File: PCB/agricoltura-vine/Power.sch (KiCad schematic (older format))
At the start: 23 parts

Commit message: Power supplies
Both power supplies redsigned around new ICs for 2A of each voltage, since we have no idea how much current peripherals will be using.
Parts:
- removed C?: GRM21BD70J226ME44L, growbox-KiCAD-Capacitors:C0805, symbol AVR-KiCAD-Lib-Capacitors:GRM21BD70J226ME44L
- removed C?: CGA3E2X7R1H104K080AA, AVR-KiCAD-Lib-Capacitors:C0603, symbol AVR-KiCAD-Lib-Capacitors:CGA3E2X7R1H104K080AA
- removed C?: GRM31CR71H475KA12L, growbox-KiCAD-Capacitors:C1206, symbol AVR-KiCAD-Lib-Capacitors:GRM31CR71H475KA12L
- removed C?: GRM32EC72A106KE05L, AVR-KiCAD-Lib-Capacitors:C1210, symbol AVR-KiCAD-Lib-Capacitors:GRM32EC72A106KE05L
- removed C?: C3216X5R1V156M160AC, AVR-KiCAD-Lib-Capacitors:C1206, symbol AVR-KiCAD-Lib-Capacitors:C3216X5R1V156M160AC
- removed C?: C2012X7R2A104K125AA, AVR-KiCAD-Lib-Capacitors:C0805, symbol AVR-KiCAD-Lib-Capacitors:C2012X7R2A104K125AA
- removed L?: SDR0403-120ML, AVR-KiCAD-Lib-Inductors:SDR0403-120ML, symbol AVR-KiCAD-Lib-Inductors:SDR0403-120ML
- removed L?: SDR0604-180YL, AVR-KiCAD-Lib-Inductors:INDP5858X480N, symbol AVR-KiCAD-Lib-Inductors:SDR0604-180YL
- removed R? (x2): RC0402FR-0722K1L, AVR-KiCAD-Lib-Resistors:R0402, symbol AVR-KiCAD-Lib-Resistors:RC0402FR-0722K1L
- removed R?: RC0402FR-07412KL, AVR-KiCAD-Lib-Resistors:R0402, symbol AVR-KiCAD-Lib-Resistors:RC0402FR-07412KL
- removed R?: RC0402FR-0751KL, AVR-KiCAD-Lib-Resistors:R0402, symbol AVR-KiCAD-Lib-Resistors:RC0402FR-0751KL
- removed R?: RC0402FR-07200KL, AVR-KiCAD-Lib-Resistors:R0402, symbol AVR-KiCAD-Lib-Resistors:RC0402FR-07200KL
- removed R?: RC0402FR-07750KL, AVR-KiCAD-Lib-Resistors:R0402, symbol AVR-KiCAD-Lib-Resistors:RC0402FR-07750KL
- removed R?: CRCW0402294KFKED, AVR-KiCAD-Lib-Resistors:R0402, symbol AVR-KiCAD-Lib-Resistors:CRCW0402294KFKED
- removed R?: RC0402FR-0788K7L, AVR-KiCAD-Lib-Resistors:R0402, symbol AVR-KiCAD-Lib-Resistors:RC0402FR-0788K7L
- removed U? (x2): TPS560430XDBVR, growbox-KiCAD-ICs:SOT-23-6_Handsoldering, symbol AVR-KiCAD-Lib-ICs:TPS560430XDBVR
- added C? (x2): GRM21BD70J226ME44L, growbox-KiCAD-Capacitors:C0805, symbol AVR-KiCAD-Lib-Capacitors:GRM21BD70J226ME44L
- added C? (x2): GRT31CR61H106KE01L, AVR-KiCAD-Lib-Capacitors:C1206, symbol AVR-KiCAD-Lib-Capacitors:GRT31CR61H106KE01L
- added C? (x2): GRT31CC81C226KE01L, AVR-KiCAD-Lib-Capacitors:C1206, symbol AVR-KiCAD-Lib-Capacitors:GRT31CC81C226KE01L
- added C? (x2): UUQ1H470MCL1GS, AVR-KiCAD-Lib-Capacitors:CP_Elec_8x10, symbol AVR-KiCAD-Lib-Capacitors:UUQ1H470MCL1GS
- added L?: SRP6540-4R7M, AVR-KiCAD-Lib-Inductors:SRP6540-4R7M, symbol AVR-KiCAD-Lib-Inductors:SRP6540-4R7M
- added L?: ASPI-0628-3R9M-T1, AVR-KiCAD-Lib-Inductors:ASPI-0628-3R9M-T1, symbol AVR-KiCAD-Lib-Inductors:ASPI-0628-3R9M-T1
- added U?: AP63205WU-7, AVR-KiCAD-Lib-ICs:SOT-23-6_Handsoldering, symbol AVR-KiCAD-Lib-ICs:AP63205WU-7
- added U?: AP63203WU-7, AVR-KiCAD-Lib-ICs:SOT-23-6_Handsoldering, symbol AVR-KiCAD-Lib-ICs:AP63203WU-7
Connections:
- wire segments 51 -> 49
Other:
- moved on the sheet: C?, D?, T?

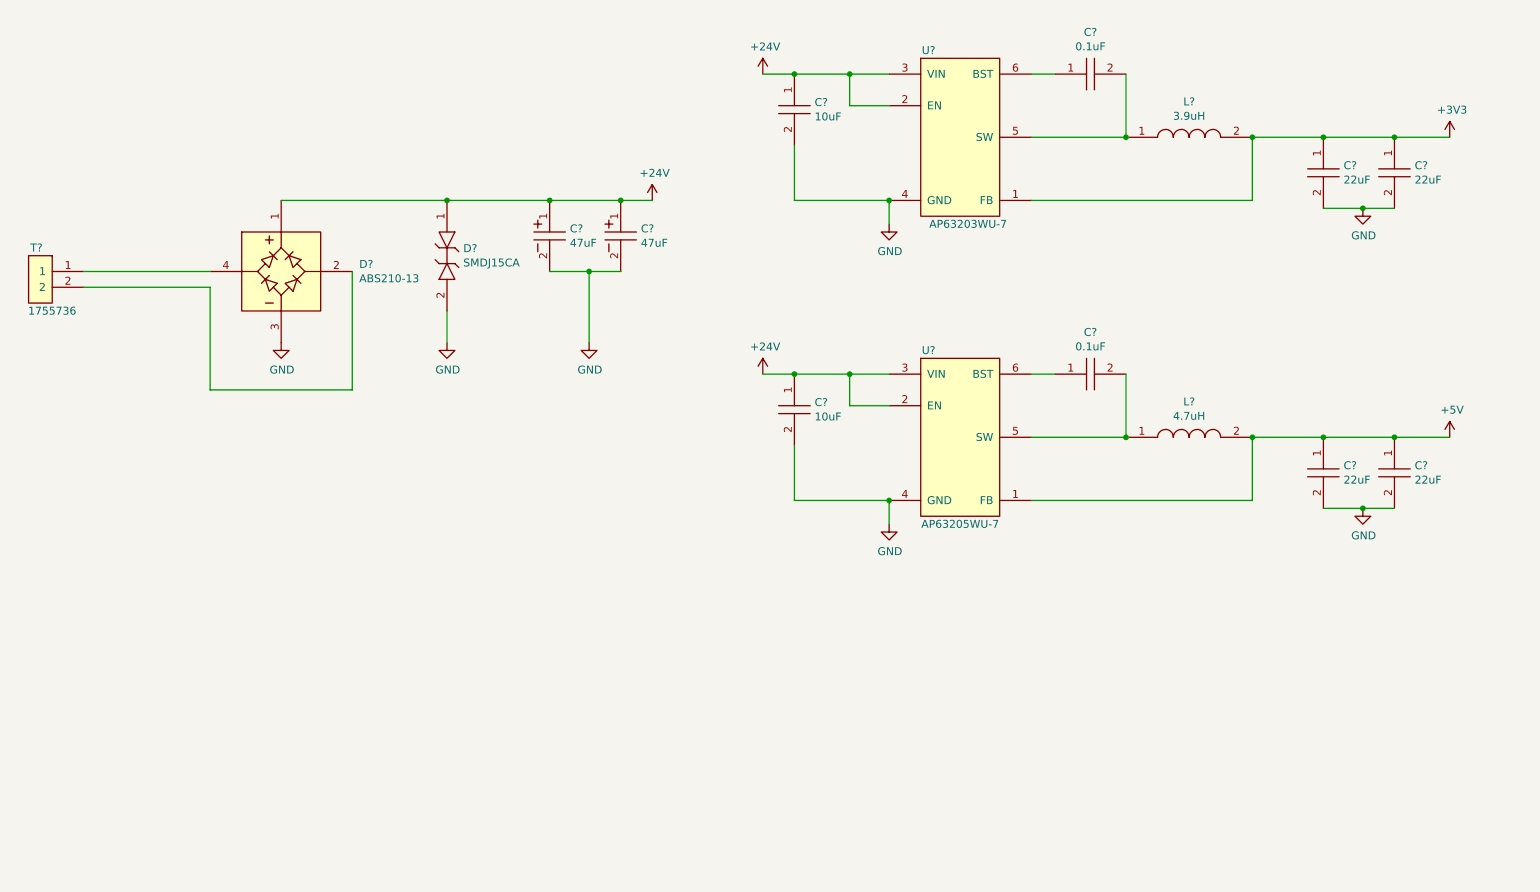
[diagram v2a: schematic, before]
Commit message: Board
Board shape defined, though subject to change. Schematic anotated and parts exported to board.
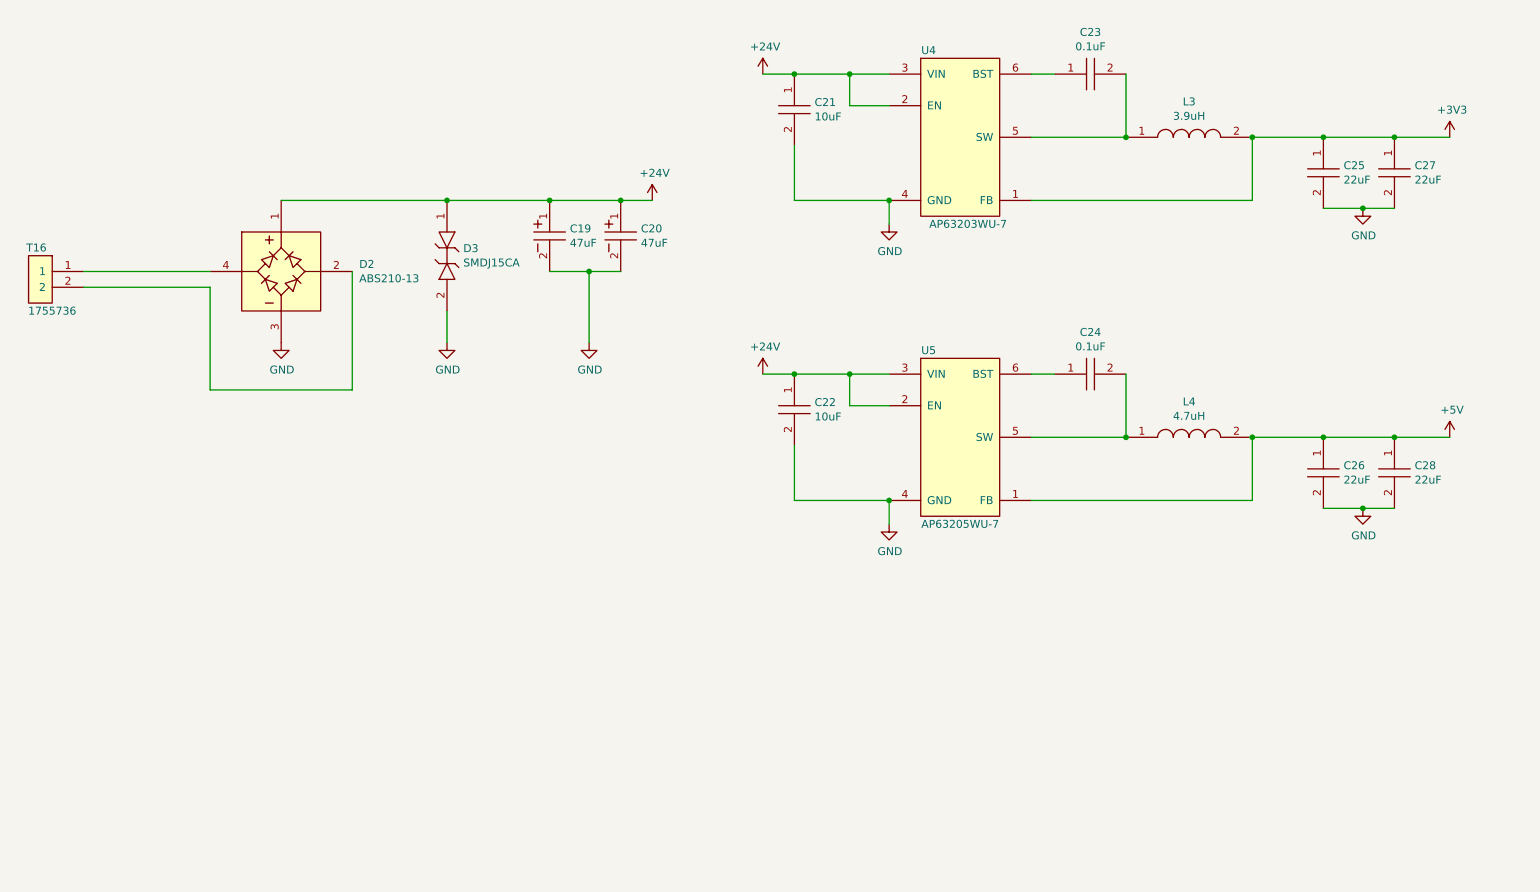
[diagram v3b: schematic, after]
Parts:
- gave numbers to parts that had none: 17
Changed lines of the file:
@@
 $EndDescr
 $Comp
-L AVR-KiCAD-Lib-Connectors:1755736 T?
+L AVR-KiCAD-Lib-Connectors:1755736 T16
 U 1 1 5EEBB45B
 P 1200 3300
-F 0 "T?" H 1300 3250 50  0000 C CNN
+F 0 "T16" H 1300 3250 50  0000 C CNN
 F 1 "1755736" H 1200 2850 50  0000 C CNN
 F 2 "growbox-KiCAD-Connectors:PhoenixContact_MSTBVA-G_02x5.08mm_Vertical" H 1000 3300 50  0001 C CNN
@@
 $EndComp
 $Comp
-L AVR-KiCAD-Lib-Diodes:ABS210-13 D?
+L AVR-KiCAD-Lib-Diodes:ABS210-13 D2
 U 1 1 5EEC167B
 P 2400 3250
-F 0 "D?" H 3144 3046 50  0000 L CNN
+F 0 "D2" H 3144 3046 50  0000 L CNN
 F 1 "ABS210-13" H 2650 4100 50  0001 C CNN
 F 2 "AVR-KiCAD-Lib-Diodes:ABS210-13" V 2800 3150 50  0001 C CNN
@@
 	3100 4250 3100 3500
 $Comp
-L power:GND #PWR?
+L power:GND #PWR028
 U 1 1 5EEC4A33
 P 2650 3950
-F 0 "#PWR?" H 2650 3700 50  0001 C CNN
+F 0 "#PWR028" H 2650 3700 50  0001 C CNN
 F 1 "GND" H 2655 3777 50  0000 C CNN
 F 2 "" H 2650 3950 50  0001 C CNN
@@
 	2650 3050 3700 3050
 $Comp
-L AVR-KiCAD-Lib-Diodes:SMDJ15CA D?
+L AVR-KiCAD-Lib-Diodes:SMDJ15CA D3
 U 1 1 5EEC73A1
 P 3700 3400
-F 0 "D?" V 3654 3503 50  0000 L CNN
+F 0 "D3" V 3654 3503 50  0000 L CNN
 F 1 "SMDJ15CA" H 3750 3600 50  0001 C CNN
 F 2 "AVR-KiCAD-Lib-Diodes:SMDJ15CA" H 3700 3300 50  0001 C CNN
@@
 $EndComp
 $Comp
-L power:GND #PWR?
+L power:GND #PWR029
 U 1 1 5EEC9E22
 P 3700 3950
-F 0 "#PWR?" H 3700 3700 50  0001 C CNN
+F 0 "#PWR029" H 3700 3700 50  0001 C CNN
 F 1 "GND" H 3705 3777 50  0000 C CNN
 F 2 "" H 3700 3950 50  0001 C CNN
@@
 	3700 3950 3700 3750
 $Comp
-L power:+24V #PWR?
+L power:+24V #PWR031
 U 1 1 5EECA5B2
 P 5000 3050
-F 0 "#PWR?" H 5000 2900 50  0001 C CNN
+F 0 "#PWR031" H 5000 2900 50  0001 C CNN
 F 1 "+24V" H 5015 3223 50  0000 C CNN
 F 2 "" H 5000 3050 50  0001 C CNN
@@
 $EndComp
 $Comp
-L AVR-KiCAD-Lib-Capacitors:C0805C104M5RACTU C?
+L AVR-KiCAD-Lib-Capacitors:C0805C104M5RACTU C23
 U 1 1 5EEE43C5
 P 7750 2250
-F 0 "C?" H 7775 2515 50  0000 C CNN
+F 0 "C23" H 7775 2515 50  0000 C CNN
 F 1 "C0805C104M5RACTU" H 7800 2450 50  0001 C CNN
 F 2 "AVR-KiCAD-Lib-Capacitors:C0805" H 7550 2250 50  0001 C CNN
@@
 $EndComp
 $Comp
-L power:+24V #PWR?
+L power:+24V #PWR033
 U 1 1 5EF02D25
 P 5700 4150
-F 0 "#PWR?" H 5700 4000 50  0001 C CNN
+F 0 "#PWR033" H 5700 4000 50  0001 C CNN
 F 1 "+24V" H 5715 4323 50  0000 C CNN
 F 2 "" H 5700 4150 50  0001 C CNN
@@
 $EndComp
 $Comp
-L power:+3V3 #PWR?
+L power:+3V3 #PWR038
 U 1 1 5EF0737A
 P 10050 2650
-F 0 "#PWR?" H 10050 2500 50  0001 C CNN
+F 0 "#PWR038" H 10050 2500 50  0001 C CNN
 F 1 "+3V3" H 10065 2823 50  0000 C CNN
 F 2 "" H 10050 2650 50  0001 C CNN
@@
 $EndComp
 $Comp
-L power:GND #PWR?
+L power:GND #PWR035
 U 1 1 5EF30432
 P 6500 5100
-F 0 "#PWR?" H 6500 4850 50  0001 C CNN
+F 0 "#PWR035" H 6500 4850 50  0001 C CNN
 F 1 "GND" H 6505 4927 50  0000 C CNN
 F 2 "" H 6500 5100 50  0001 C CNN
@@
 $EndComp
 $Comp
-L power:+5V #PWR?
+L power:+5V #PWR039
 U 1 1 5EF3A247
 P 10050 4550
-F 0 "#PWR?" H 10050 4400 50  0001 C CNN
+F 0 "#PWR039" H 10050 4400 50  0001 C CNN
 F 1 "+5V" H 10065 4723 50  0000 C CNN
 F 2 "" H 10050 4550 50  0001 C CNN
@@
 $EndComp
 $Comp
-L AVR-KiCAD-Lib-Capacitors:C2012X7R2A104K125AA C?
+L AVR-KiCAD-Lib-Capacitors:C2012X7R2A104K125AA C24
 U 1 1 5EF56247
 P 7750 4150
-F 0 "C?" H 7775 4415 50  0000 C CNN
+F 0 "C24" H 7775 4415 50  0000 C CNN
 F 1 "C2012X7R2A104K125AA" H 7800 4350 50  0001 C CNN
 F 2 "AVR-KiCAD-Lib-Capacitors:C0805" H 7550 4150 50  0001 C CNN
@@
 $EndComp
 $Comp
-L AVR-KiCAD-Lib-Capacitors:GRM21BD70J226ME44L C?
+L AVR-KiCAD-Lib-Capacitors:GRM21BD70J226ME44L C25
 U 1 1 5EEE8244
 P 9250 2850
-F 0 "C?" V 9229 2978 50  0000 L CNN
+F 0 "C25" V 9229 2978 50  0000 L CNN
 F 1 "GRM21BD70J226ME44L" H 9300 3050 50  0001 C CNN
 F 2 "growbox-KiCAD-Capacitors:C0805" H 9050 2850 50  0001 C CNN
@@
 $EndComp
 $Comp
-L AVR-KiCAD-Lib-Capacitors:GRM21BD70J226ME44L C?
+L AVR-KiCAD-Lib-Capacitors:GRM21BD70J226ME44L C27
 U 1 1 5EEE8263
 P 9700 2850
-F 0 "C?" V 9679 2978 50  0000 L CNN
+F 0 "C27" V 9679 2978 50  0000 L CNN
 F 1 "GRM21BD70J226ME44L" H 9750 3050 50  0001 C CNN
 F 2 "growbox-KiCAD-Capacitors:C0805" H 9500 2850 50  0001 C CNN
@@
 $EndComp
 $Comp
-L AVR-KiCAD-Lib-ICs:AP63205WU-7 U?
+L AVR-KiCAD-Lib-ICs:AP63205WU-7 U5
 U 1 1 5EEE9657
 P 6700 4050
-F 0 "U?" H 6750 4100 50  0000 C CNN
+F 0 "U5" H 6750 4100 50  0000 C CNN
 F 1 "AP63205WU-7" H 6750 4150 50  0001 C CNN
 F 2 "AVR-KiCAD-Lib-ICs:SOT-23-6_Handsoldering" H 5900 4700 50  0001 C CNN
@@
 $EndComp
 $Comp
-L AVR-KiCAD-Lib-Inductors:SRP6540-4R7M L?
+L AVR-KiCAD-Lib-Inductors:SRP6540-4R7M L4
 U 1 1 5EEF14B5
 P 8400 4550
-F 0 "L?" H 8400 4775 50  0000 C CNN
+F 0 "L4" H 8400 4775 50  0000 C CNN
 F 1 "SRP6540-4R7M" H 8450 4750 50  0001 C CNN
 F 2 "AVR-KiCAD-Lib-Inductors:SRP6540-4R7M" H 8400 4550 50  0001 C CNN
@@
 	6250 4150 6500 4150
 $Comp
-L power:GND #PWR?
+L power:GND #PWR037
 U 1 1 5EF0BF07
 P 9500 5000
-F 0 "#PWR?" H 9500 4750 50  0001 C CNN
+F 0 "#PWR037" H 9500 4750 50  0001 C CNN
 F 1 "GND" H 9505 4827 50  0000 C CNN
 F 2 "" H 9500 5000 50  0001 C CNN
@@
 	8800 4550 9250 4550
 $Comp
-L AVR-KiCAD-Lib-Capacitors:GRT31CR61H106KE01L C?
+L AVR-KiCAD-Lib-Capacitors:GRT31CR61H106KE01L C22
 U 1 1 5EF20097
 P 5900 4350
-F 0 "C?" V 5879 4478 50  0000 L CNN
+F 0 "C22" V 5879 4478 50  0000 L CNN
 F 1 "GRT31CR61H106KE01L" H 5950 4550 50  0001 C CNN
 F 2 "AVR-KiCAD-Lib-Capacitors:C1206" H 5700 4350 50  0001 C CNN
@@
 Connection ~ 6500 4950
 $Comp
-L AVR-KiCAD-Lib-Capacitors:GRT31CC81C226KE01L C?
+L AVR-KiCAD-Lib-Capacitors:GRT31CC81C226KE01L C26
 U 1 1 5EF26633
 P 9250 4750
-F 0 "C?" V 9229 4878 50  0000 L CNN
+F 0 "C26" V 9229 4878 50  0000 L CNN
 F 1 "GRT31CC81C226KE01L" H 9300 4950 50  0001 C CNN
 F 2 "AVR-KiCAD-Lib-Capacitors:C1206" H 9050 4750 50  0001 C CNN
@@
 	9250 4550 9700 4550
 $Comp
-L AVR-KiCAD-Lib-Capacitors:GRT31CC81C226KE01L C?
+L AVR-KiCAD-Lib-Capacitors:GRT31CC81C226KE01L C28
 U 1 1 5EF27C99
 P 9700 4750
-F 0 "C?" V 9679 4878 50  0000 L CNN
+F 0 "C28" V 9679 4878 50  0000 L CNN
 F 1 "GRT31CC81C226KE01L" H 9750 4950 50  0001 C CNN
 F 2 "AVR-KiCAD-Lib-Capacitors:C1206" H 9500 4750 50  0001 C CNN
@@
 	9700 4550 10050 4550
 $Comp
-L AVR-KiCAD-Lib-ICs:AP63203WU-7 U?
+L AVR-KiCAD-Lib-ICs:AP63203WU-7 U4
 U 1 1 5EF29865
 P 6700 2150
-F 0 "U?" H 6750 2200 50  0000 C CNN
+F 0 "U4" H 6750 2200 50  0000 C CNN
 F 1 "AP63203WU-7" H 6750 2250 50  0001 C CNN
 F 2 "AVR-KiCAD-Lib-ICs:SOT-23-6_Handsoldering" H 5900 2800 50  0001 C CNN
@@
 $EndComp
 $Comp
-L power:+24V #PWR?
+L power:+24V #PWR032
 U 1 1 5EF2E19F
 P 5700 2250
-F 0 "#PWR?" H 5700 2100 50  0001 C CNN
+F 0 "#PWR032" H 5700 2100 50  0001 C CNN
 F 1 "+24V" H 5715 2423 50  0000 C CNN
 F 2 "" H 5700 2250 50  0001 C CNN
@@
 $EndComp
 $Comp
-L power:GND #PWR?
+L power:GND #PWR034
 U 1 1 5EF2E1A5
 P 6500 3200
-F 0 "#PWR?" H 6500 2950 50  0001 C CNN
+F 0 "#PWR034" H 6500 2950 50  0001 C CNN
 F 1 "GND" H 6505 3027 50  0000 C CNN
 F 2 "" H 6500 3200 50  0001 C CNN
@@
 	6500 3200 6500 3050
 $Comp
-L AVR-KiCAD-Lib-Capacitors:GRT31CR61H106KE01L C?
+L AVR-KiCAD-Lib-Capacitors:GRT31CR61H106KE01L C21
 U 1 1 5EF2E1E9
 P 5900 2450
-F 0 "C?" V 5879 2578 50  0000 L CNN
+F 0 "C21" V 5879 2578 50  0000 L CNN
 F 1 "GRT31CR61H106KE01L" H 5950 2650 50  0001 C CNN
 F 2 "AVR-KiCAD-Lib-Capacitors:C1206" H 5700 2450 50  0001 C CNN
@@
 	7550 2250 7400 2250
 $Comp
-L AVR-KiCAD-Lib-Inductors:ASPI-0628-3R9M-T1 L?
+L AVR-KiCAD-Lib-Inductors:ASPI-0628-3R9M-T1 L3
 U 1 1 5EF379D3
 P 8400 2650
-F 0 "L?" H 8400 2875 50  0000 C CNN
+F 0 "L3" H 8400 2875 50  0000 C CNN
 F 1 "ASPI-0628-3R9M-T1" H 8450 2850 50  0001 C CNN
 F 2 "AVR-KiCAD-Lib-Inductors:ASPI-0628-3R9M-T1" H 8400 2650 50  0001 C CNN
@@
 	8800 3050 8800 2650
 $Comp
-L power:GND #PWR?
+L power:GND #PWR036
 U 1 1 5EF3F029
 P 9500 3100
-F 0 "#PWR?" H 9500 2850 50  0001 C CNN
+F 0 "#PWR036" H 9500 2850 50  0001 C CNN
 F 1 "GND" H 9505 2927 50  0000 C CNN
 F 2 "" H 9500 3100 50  0001 C CNN
@@
 	3700 3050 4350 3050
 $Comp
-L AVR-KiCAD-Lib-Capacitors:UUQ1H470MCL1GS C?
+L AVR-KiCAD-Lib-Capacitors:UUQ1H470MCL1GS C19
 U 1 1 5EF765E1
 P 4350 3250
-F 0 "C?" V 4329 3378 50  0000 L CNN
+F 0 "C19" V 4329 3378 50  0000 L CNN
 F 1 "UUQ1H470MCL1GS" H 4400 3450 50  0001 C CNN
 F 2 "AVR-KiCAD-Lib-Capacitors:CP_Elec_8x10" H 4150 3250 50  0001 C CNN
@@
 	4350 3050 4800 3050
 $Comp
-L AVR-KiCAD-Lib-Capacitors:UUQ1H470MCL1GS C?
+L AVR-KiCAD-Lib-Capacitors:UUQ1H470MCL1GS C20
 U 1 1 5EF7802F
 P 4800 3250
-F 0 "C?" V 4779 3378 50  0000 L CNN
+F 0 "C20" V 4779 3378 50  0000 L CNN
 F 1 "UUQ1H470MCL1GS" H 4850 3450 50  0001 C CNN
 F 2 "AVR-KiCAD-Lib-Capacitors:CP_Elec_8x10" H 4600 3250 50  0001 C CNN
@@
 	4800 3050 5000 3050
 $Comp
-L power:GND #PWR?
+L power:GND #PWR030
 U 1 1 5EF78FAF
 P 4600 3950
-F 0 "#PWR?" H 4600 3700 50  0001 C CNN
+F 0 "#PWR030" H 4600 3700 50  0001 C CNN
 F 1 "GND" H 4605 3777 50  0000 C CNN
 F 2 "" H 4600 3950 50  0001 C CNN
